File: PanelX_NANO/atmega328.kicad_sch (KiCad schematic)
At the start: 8 parts

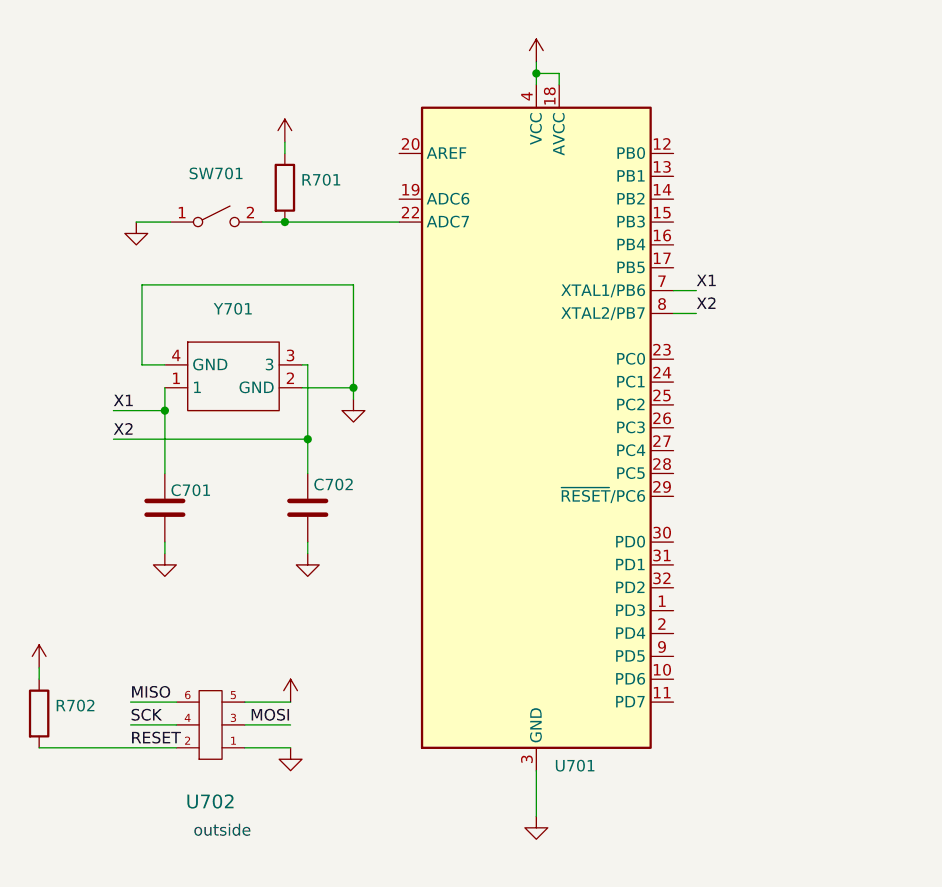
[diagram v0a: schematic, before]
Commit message: Deleted zip files from repo
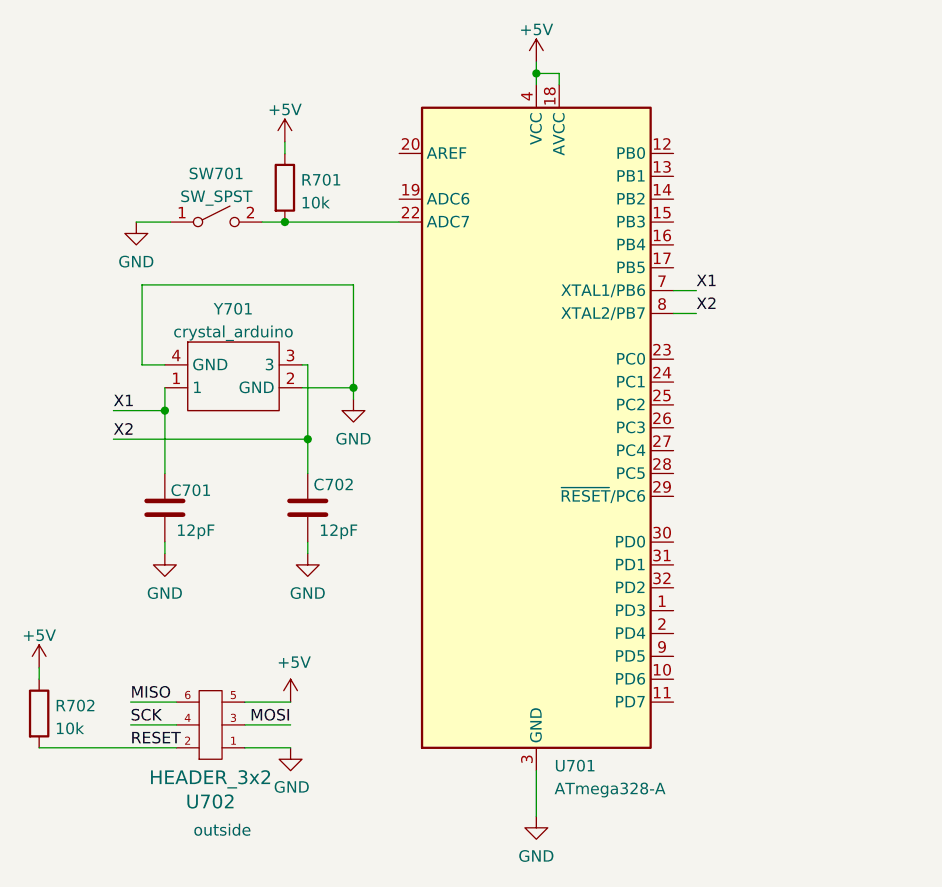
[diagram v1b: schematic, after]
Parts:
- C701, C702: value (none) -> 12pF; footprint (none) -> Capacitor_SMD:C_0805_2012Metric_Pad1.18x1.45mm_HandSolder
- R701, R702: value (none) -> 10k; footprint (none) -> Resistor_SMD:R_0603_1608Metric_Pad0.98x0.95mm_HandSolder
- SW701: value (none) -> SW_SPST; footprint (none) -> Button_Switch_SMD:SW_SPST_SKQG_WithStem
- U701: value (none) -> ATmega328-A; footprint (none) -> Package_QFP:TQFP-32_7x7mm_P0.8mm
- U702: value (none) -> HEADER_3x2; footprint (none) -> Connector_PinSocket_1.27mm:PinSocket_2x03_P1.27mm_Vertical
- Y701: value (none) -> crystal_arduino; footprint (none) -> custom_kicad_lib_sk:crystal_arduino
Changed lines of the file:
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@@
       (effects (font (size 1.27 1.27)) (justify right))
     )
-    (property "Value" "" (id 1) (at 50.165 97.79 0)
+    (property "Value" "12pF" (id 1) (at 50.165 97.79 0)
       (effects (font (size 1.27 1.27)) (justify right))
     )
-    (property "Footprint" "" (id 2) (at 47.9298 91.44 0)
+    (property "Footprint" "Capacitor_SMD:C_0805_2012Metric_Pad1.18x1.45mm_HandSolder" (id 2) (at 47.9298 91.44 0)
       (effects (font (size 1.27 1.27)) hide)
     )
@@
       (effects (font (size 1.27 1.27)) hide)
     )
-    (property "Value" "" (id 1) (at 64.77 104.7734 0))
+    (property "Value" "GND" (id 1) (at 64.77 104.7734 0))
     (property "Footprint" "" (id 2) (at 64.77 100.33 0)
       (effects (font (size 1.27 1.27)) hide)
@@
       (effects (font (size 1.27 1.27)) hide)
     )
-    (property "Value" "" (id 1) (at 45.72 67.9434 0))
+    (property "Value" "GND" (id 1) (at 45.72 67.9434 0))
     (property "Footprint" "" (id 2) (at 45.72 63.5 0)
       (effects (font (size 1.27 1.27)) hide)
@@
       (effects (font (size 1.27 1.27)) hide)
     )
-    (property "Value" "" (id 1) (at 63.246 112.4458 0))
+    (property "Value" "+5V" (id 1) (at 63.246 112.4458 0))
     (property "Footprint" "" (id 2) (at 62.865 116.84 0)
       (effects (font (size 1.27 1.27)) hide)
@@
       (effects (font (size 1.27 1.27)) (justify right))
     )
-    (property "Value" "" (id 1) (at 66.04 97.79 0)
+    (property "Value" "12pF" (id 1) (at 66.04 97.79 0)
       (effects (font (size 1.27 1.27)) (justify right))
     )
-    (property "Footprint" "" (id 2) (at 63.8048 91.44 0)
+    (property "Footprint" "Capacitor_SMD:C_0805_2012Metric_Pad1.18x1.45mm_HandSolder" (id 2) (at 63.8048 91.44 0)
       (effects (font (size 1.27 1.27)) hide)
     )
@@
       (effects (font (size 1.27 1.27)) (justify left))
     )
-    (property "Value" "" (id 1) (at 92.1894 126.4873 0)
-      (effects (font (size 1.27 1.27)) (justify left))
-    )
-    (property "Footprint" "" (id 2) (at 90.17 86.36 0)
+    (property "Value" "ATmega328-A" (id 1) (at 92.1894 126.4873 0)
+      (effects (font (size 1.27 1.27)) (justify left))
+    )
+    (property "Footprint" "Package_QFP:TQFP-32_7x7mm_P0.8mm" (id 2) (at 90.17 86.36 0)
       (effects (font (size 1.27 1.27) italic) hide)
     )
@@
       (effects (font (size 1.27 1.27)) hide)
     )
-    (property "Value" "" (id 1) (at 90.17 133.9834 0))
+    (property "Value" "GND" (id 1) (at 90.17 133.9834 0))
     (property "Footprint" "" (id 2) (at 90.17 129.54 0)
       (effects (font (size 1.27 1.27)) hide)
@@
     (in_bom yes) (on_board yes) (fields_autoplaced)
     (property "Reference" "SW701" (id 0) (at 54.61 58.1492 0))
-    (property "Value" "" (id 1) (at 54.61 60.6861 0))
-    (property "Footprint" "" (id 2) (at 54.61 63.5 0)
+    (property "Value" "SW_SPST" (id 1) (at 54.61 60.6861 0))
+    (property "Footprint" "Button_Switch_SMD:SW_SPST_SKQG_WithStem" (id 2) (at 54.61 63.5 0)
       (effects (font (size 1.27 1.27)) hide)
     )
@@
       (effects (font (size 1.27 1.27)) hide)
     )
-    (property "Value" "" (id 1) (at 69.85 87.6284 0))
+    (property "Value" "GND" (id 1) (at 69.85 87.6284 0))
     (property "Footprint" "" (id 2) (at 69.85 83.185 0)
       (effects (font (size 1.27 1.27)) hide)
@@
     (in_bom yes) (on_board yes) (fields_autoplaced)
     (property "Reference" "Y701" (id 0) (at 56.515 73.186 0))
-    (property "Value" "" (id 1) (at 56.515 75.7229 0))
-    (property "Footprint" "" (id 2) (at 59.055 88.265 0)
+    (property "Value" "crystal_arduino" (id 1) (at 56.515 75.7229 0))
+    (property "Footprint" "custom_kicad_lib_sk:crystal_arduino" (id 2) (at 59.055 88.265 0)
       (effects (font (size 1.27 1.27)) hide)
     )
@@
       (effects (font (size 1.27 1.27)) hide)
     )
-    (property "Value" "" (id 1) (at 34.925 109.4542 0))
+    (property "Value" "+5V" (id 1) (at 34.925 109.4542 0))
     (property "Footprint" "" (id 2) (at 34.925 113.03 0)
       (effects (font (size 1.27 1.27)) hide)
@@
       (effects (font (size 1.27 1.27)) (justify left))
     )
-    (property "Value" "" (id 1) (at 64.008 61.3922 0)
-      (effects (font (size 1.27 1.27)) (justify left))
-    )
-    (property "Footprint" "" (id 2) (at 60.452 59.69 90)
+    (property "Value" "10k" (id 1) (at 64.008 61.3922 0)
+      (effects (font (size 1.27 1.27)) (justify left))
+    )
+    (property "Footprint" "Resistor_SMD:R_0603_1608Metric_Pad0.98x0.95mm_HandSolder" (id 2) (at 60.452 59.69 90)
       (effects (font (size 1.27 1.27)) hide)
     )
@@
       (effects (font (size 1.27 1.27)) hide)
     )
-    (property "Value" "" (id 1) (at 90.17 42.1442 0))
+    (property "Value" "+5V" (id 1) (at 90.17 42.1442 0))
     (property "Footprint" "" (id 2) (at 90.17 45.72 0)
       (effects (font (size 1.27 1.27)) hide)
@@
       (effects (font (size 1.27 1.27)) hide)
     )
-    (property "Value" "" (id 1) (at 48.895 104.7734 0))
+    (property "Value" "GND" (id 1) (at 48.895 104.7734 0))
     (property "Footprint" "" (id 2) (at 48.895 100.33 0)
       (effects (font (size 1.27 1.27)) hide)
@@
       (effects (font (size 1.524 1.524)))
     )
-    (property "Value" "" (id 1) (at 53.975 125.2474 0)
+    (property "Value" "HEADER_3x2" (id 1) (at 53.975 125.2474 0)
       (effects (font (size 1.524 1.524)))
     )
-    (property "Footprint" "" (id 2) (at 53.975 119.38 0)
+    (property "Footprint" "Connector_PinSocket_1.27mm:PinSocket_2x03_P1.27mm_Vertical" (id 2) (at 53.975 119.38 0)
       (effects (font (size 1.524 1.524)) hide)
     )
@@
       (effects (font (size 1.27 1.27)) hide)
     )
-    (property "Value" "" (id 1) (at 62.23 51.0342 0))
+    (property "Value" "+5V" (id 1) (at 62.23 51.0342 0))
     (property "Footprint" "" (id 2) (at 62.23 54.61 0)
       (effects (font (size 1.27 1.27)) hide)
@@
       (effects (font (size 1.27 1.27)) hide)
     )
-    (property "Value" "" (id 1) (at 62.992 126.3142 0))
+    (property "Value" "GND" (id 1) (at 62.992 126.3142 0))
     (property "Footprint" "" (id 2) (at 62.865 121.92 0)
       (effects (font (size 1.27 1.27)) hide)
@@
       (effects (font (size 1.27 1.27)) (justify left))
     )
-    (property "Value" "" (id 1) (at 36.703 119.8122 0)
-      (effects (font (size 1.27 1.27)) (justify left))
-    )
-    (property "Footprint" "" (id 2) (at 33.147 118.11 90)
-      (effects (font (size 1.27 1.27)) hide)
-    )
+    (property "Value" "10k" (id 1) (at 36.703 119.8122 0)
+      (effects (font (size 1.27 1.27)) (justify left))
+    )
+    (property "Footprint" "Resistor_SMD:R_0603_1608Metric_Pad0.98x0.95mm_HandSolder" (id 2) (at 33.147 118.11 90)
+      (effects (font (size 1.27 1.27)) hide)
+    )

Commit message: I picked a suitable connector. I will use plain 2x12 female n male connectors for the b2b connector. Death to flatcables! The RJ12 connector still goed on the panel carrier board. I will look for vertical SMD variant
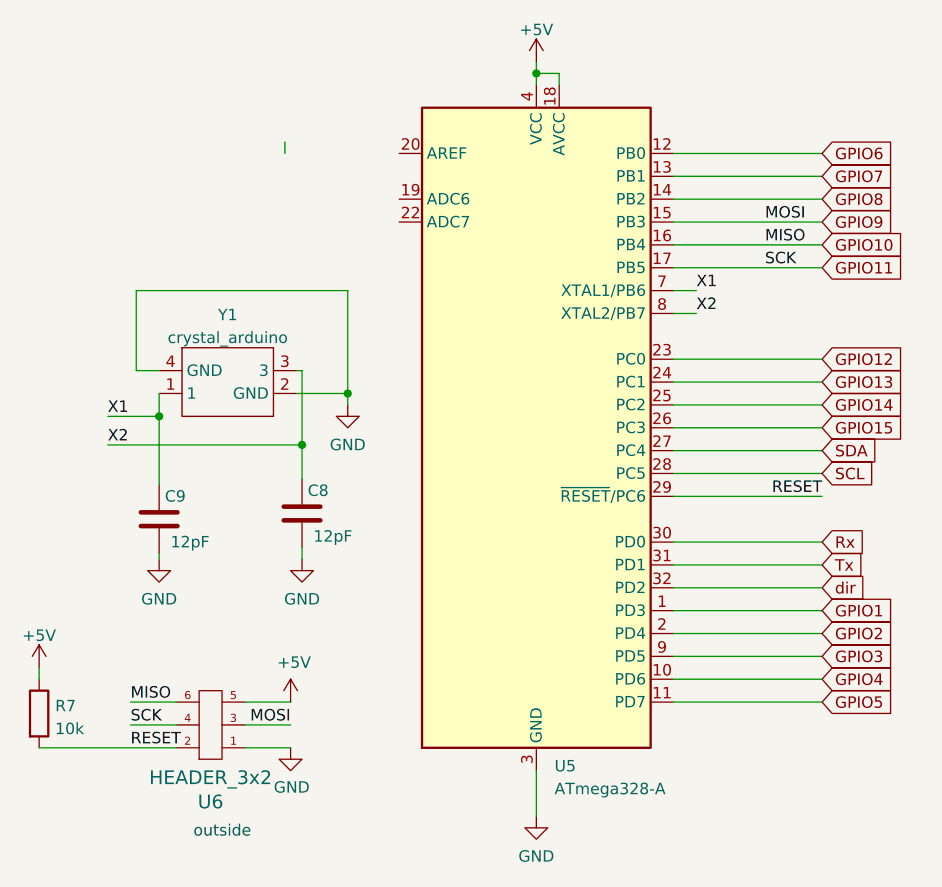
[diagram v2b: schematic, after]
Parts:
- removed C701: 12pF, Capacitor_SMD:C_0805_2012Metric_Pad1.18x1.45mm_HandSolder, symbol Device:C
- removed R701: 10k, Resistor_SMD:R_0603_1608Metric_Pad0.98x0.95mm_HandSolder, symbol Device:R
- removed SW701: SW_SPST, Button_Switch_SMD:SW_SPST_SKQG_WithStem, symbol Switch:SW_SPST
- added C9: 12pF, Capacitor_SMD:C_0603_1608Metric_Pad1.08x0.95mm_HandSolder, symbol Device:C
- C8: renamed from C702; footprint Capacitor_SMD:C_0805_2012Metric_Pad1.18x1.45mm_HandSolder -> Capacitor_SMD:C_0603_1608Metric_Pad1.08x0.95mm_HandSolder
- renumbered R702 to R7, U701 to U5, U702 to U6, Y701 to Y1
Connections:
- net MISO is gone; now on net GPIO10: U6.6
- net MOSI is gone; now on net GPIO9: U6.3
- net SCK is gone; now on net GPIO11: U6.4
- net GND: now also C9.1
- net RESET: now also U5.29 (~{RESET}/PC6)
- net X1: now also C9.2
- net GPIO1: now reaches U5.1 (PD3)
- net GPIO4: now reaches U5.10 (PD6)
- net GPIO5: now reaches U5.11 (PD7)
- net GPIO6: now reaches U5.12 (PB0)
- net GPIO7: now reaches U5.13 (PB1)
- net GPIO8: now reaches U5.14 (PB2)
- net GPIO9: now reaches U5.15 (PB3)
- net GPIO10: now reaches U5.16 (PB4)
- net GPIO11: now reaches U5.17 (PB5)
- net GPIO2: now reaches U5.2 (PD4)
- net GPIO12: now reaches U5.23 (PC0)
- net GPIO13: now reaches U5.24 (PC1)
- net GPIO14: now reaches U5.25 (PC2)
- net GPIO15: now reaches U5.26 (PC3)
- net SDA: now reaches U5.27 (PC4)
- net SCL: now reaches U5.28 (PC5)
- net Rx: now reaches U5.30 (PD0)
- net Tx: now reaches U5.31 (PD1)
- net dir: now reaches U5.32 (PD2)
- net GPIO3: now reaches U5.9 (PD5)
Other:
- moved on the sheet: C8, Y1
